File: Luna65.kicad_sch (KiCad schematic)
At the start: 169 parts, among them J1 TYPE-C-31-M12_13, SW0 SW_Push, SW1 Esc, SW10 9, SW11 0, SW12 -, SW13 =, SW14 BSP_200, SW15 Del, SW16 Tab_150, SW17 Q, SW18 W, SW19 E, SW2 1, SW20 R, SW21 T, SW22 Y, SW23 U, SW24 I, SW25 O, SW26 P, SW27 [, SW28 ], SW29 \_150, SW3 2, SW30 Home, SW31 Caps_175, SW32 A, SW33 S, SW34 D, SW35 F, SW36 G, SW37 H, SW38 J, SW39 K, SW4 3, SW40 L, SW41 ;, SW42 ', SW43 Ent_225, SW44 PgUp, SW45 LShft_225, SW46 Z, SW47 X, SW48 C, SW49 V, SW5 4, SW50 B, SW51 N, SW52 M, SW53 ,, SW54 ., SW55 /, SW56 RShft_175, SW57 Up, SW58 End, SW59 LCtrl_125, SW6 5, SW60 Win_125, SW61 LAlt_125, SW62 Space_625, SW63 RAlt, SW64 Fn, SW65 RCtrl, SW66 Left, SW67 Down, SW68 Right, SW7 6, SW8 7, SW9 8, U1 ATmega32U4-AU, U2 USBLC6-2SC6, Y1 16MHz

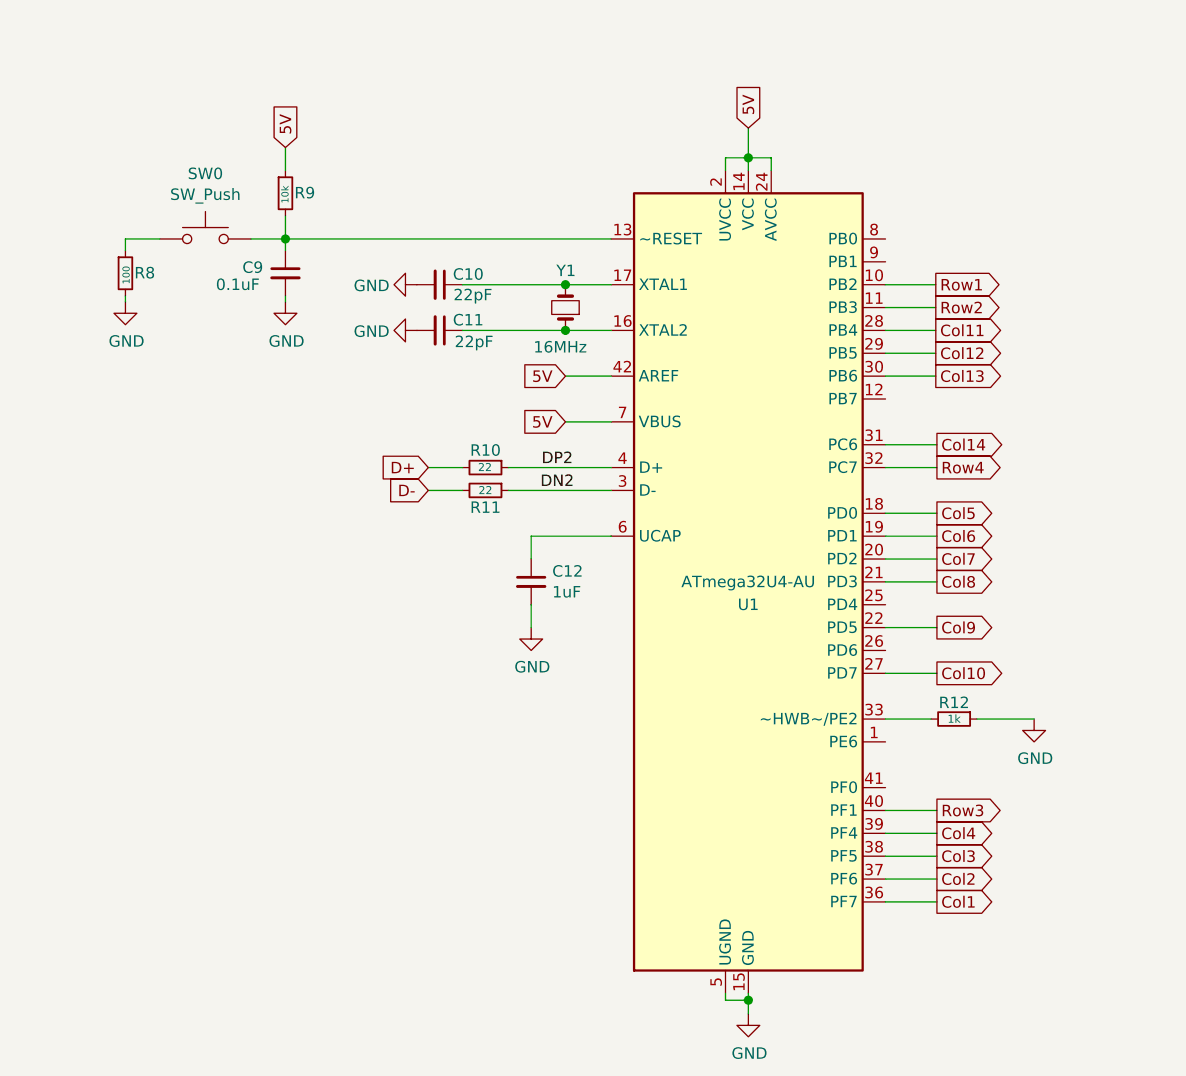
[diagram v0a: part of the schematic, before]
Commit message: Completed routing
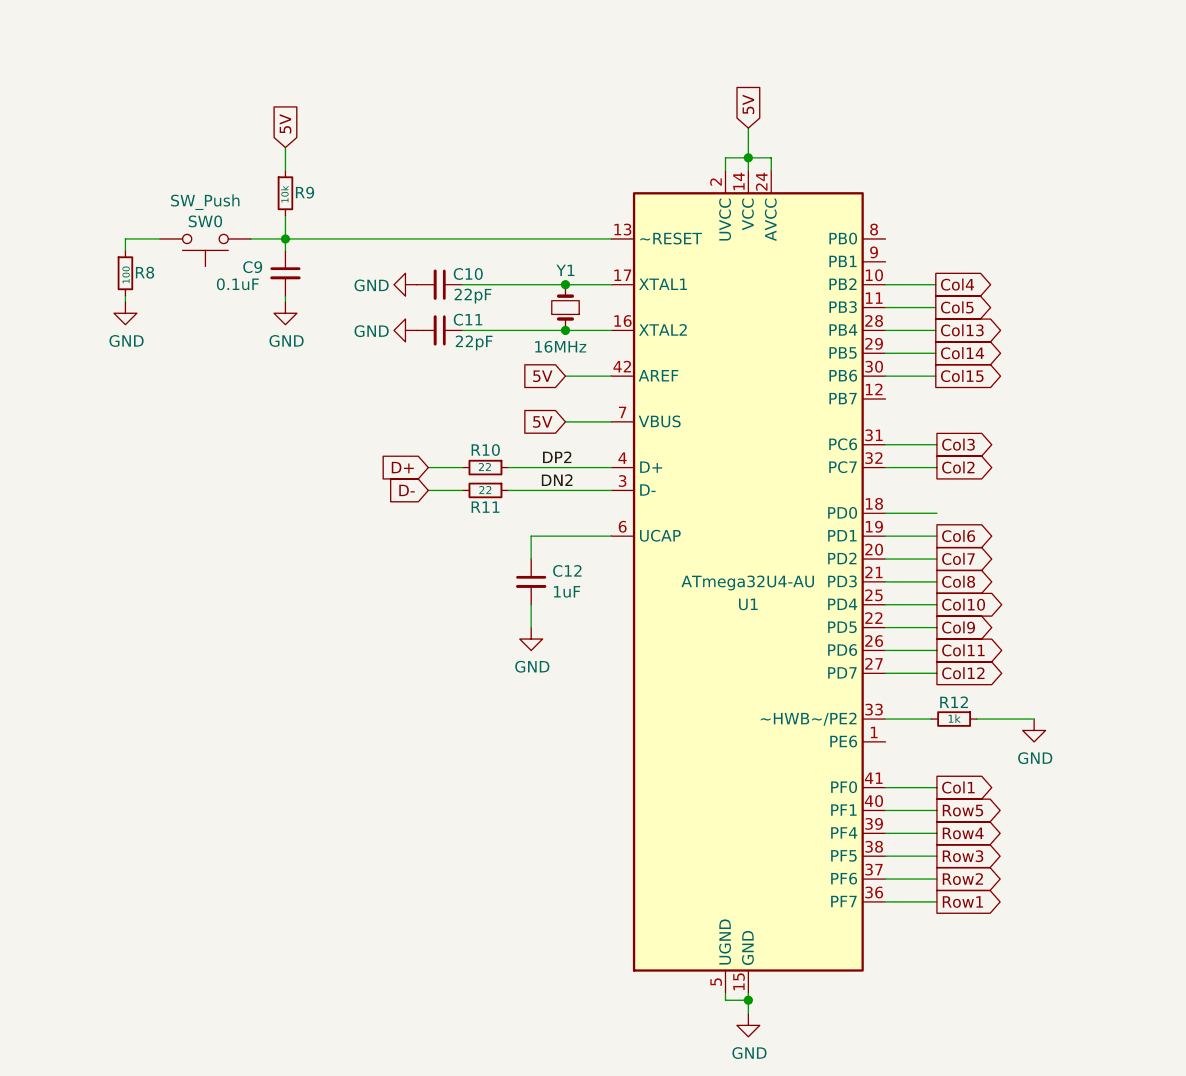
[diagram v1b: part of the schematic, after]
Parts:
- SW0: footprint Button_Switch_SMD:SW_Push_1P1T_NO_CK_KMR2 -> acheron_Hardware:K2-1187SQ-A4SW-06
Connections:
- net Col1: now also U1.41 (PF0); no longer U1.36 (PF7)
- net Col10: now also U1.25 (PD4); no longer U1.27 (PD7)
- net Col11: now also U1.26 (PD6); no longer U1.28 (PB4)
- net Col12: now also U1.27 (PD7); no longer U1.29 (PB5)
- net Col13: now also U1.28 (PB4); no longer U1.30 (PB6)
- net Col14: now also U1.29 (PB5); no longer U1.31 (PC6)
- net Col15: now also U1.30 (PB6)
- net Col2: now also U1.32 (PC7); no longer U1.37 (PF6)
- net Col3: now also U1.31 (PC6); no longer U1.38 (PF5)
- net Col4: now also U1.10 (PB2); no longer U1.39 (PF4)
- net Col5: now also U1.11 (PB3); no longer U1.18 (PD0)
- net Row1: now also U1.36 (PF7); no longer U1.10 (PB2)
- net Row2: now also U1.37 (PF6); no longer U1.11 (PB3)
- net Row3: now also U1.38 (PF5); no longer U1.40 (PF1)
- net Row4: now also U1.39 (PF4); no longer U1.32 (PC7)
- net Row5: now also U1.40 (PF1)
- net at C9.1, R9.2, U1.13 (~RESET): now also SW0.1; no longer SW0.2
- net at R8.1: now also SW0.2; no longer SW0.1
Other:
- moved on the sheet: SW0
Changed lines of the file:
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@@
     (stroke (width 0) (type solid) (color 0 0 0 0))
   )
+  (wire (pts (xy 268.986 223.393) (xy 274.701 223.393))
+    (stroke (width 0) (type solid) (color 0 0 0 0))
+  )
   (wire (pts (xy 268.986 225.933) (xy 274.701 225.933))
     (stroke (width 0) (type solid) (color 0 0 0 0))
   )
+  (wire (pts (xy 268.986 228.473) (xy 274.701 228.473))
+    (stroke (width 0) (type solid) (color 0 0 0 0))
+  )
   (wire (pts (xy 268.986 231.013) (xy 274.701 231.013))
     (stroke (width 0) (type solid) (color 0 0 0 0))
@@
     (stroke (width 0) (type solid) (color 0 0 0 0))
   )
+  (wire (pts (xy 268.986 243.713) (xy 274.701 243.713))
+    (stroke (width 0) (type solid) (color 0 0 0 0))
+  )
   (wire (pts (xy 268.986 246.253) (xy 274.701 246.253))
     (stroke (width 0) (type solid) (color 0 0 0 0))
@@
     )
   )
-  (global_label "Row1" (shape output) (at 274.574 187.833 0) (fields_autoplaced)
+  (global_label "Col4" (shape output) (at 274.574 187.833 0) (fields_autoplaced)
     (effects (font (size 1.27 1.27)) (justify left))
-    (property "Intersheet References" "${INTERSHEET_REFS}" (id 0) (at 281.9461 187.7536 0)
+    (property "Intersheet References" "${INTERSHEET_REFS}" (id 0) (at 281.2809 187.7536 0)
       (effects (font (size 1.27 1.27)) (justify left) hide)
     )
   )
-  (global_label "Row2" (shape output) (at 274.574 190.373 0) (fields_autoplaced)
+  (global_label "Col5" (shape output) (at 274.574 190.373 0) (fields_autoplaced)
     (effects (font (size 1.27 1.27)) (justify left))
-    (property "Intersheet References" "${INTERSHEET_REFS}" (id 0) (at 281.9461 190.2936 0)
+    (property "Intersheet References" "${INTERSHEET_REFS}" (id 0) (at 281.2809 190.2936 0)
       (effects (font (size 1.27 1.27)) (justify left) hide)
     )
   )
-  (global_label "Col11" (shape output) (at 274.574 192.913 0) (fields_autoplaced)
+  (global_label "Col13" (shape output) (at 274.574 192.913 0) (fields_autoplaced)
     (effects (font (size 1.27 1.27)) (justify left))
     (property "Intersheet References" "${INTERSHEET_REFS}" (id 0) (at 282.4904 192.8336 0)
@@
     )
   )
-  (global_label "Col12" (shape output) (at 274.574 195.453 0) (fields_autoplaced)
+  (global_label "Col14" (shape output) (at 274.574 195.453 0) (fields_autoplaced)
     (effects (font (size 1.27 1.27)) (justify left))
     (property "Intersheet References" "${INTERSHEET_REFS}" (id 0) (at 282.4904 195.3736 0)
@@
     )
   )
-  (global_label "Col13" (shape output) (at 274.574 197.993 0) (fields_autoplaced)
+  (global_label "Col15" (shape output) (at 274.574 197.993 0) (fields_autoplaced)
     (effects (font (size 1.27 1.27)) (justify left))
     (property "Intersheet References" "${INTERSHEET_REFS}" (id 0) (at 282.4904 197.9136 0)
@@
     )
   )
-  (global_label "Col14" (shape output) (at 274.701 205.613 0) (fields_autoplaced)
+  (global_label "Col3" (shape output) (at 274.701 205.613 0) (fields_autoplaced)
     (effects (font (size 1.27 1.27)) (justify left))
-    (property "Intersheet References" "${INTERSHEET_REFS}" (id 0) (at 282.6174 205.5336 0)
+    (property "Intersheet References" "${INTERSHEET_REFS}" (id 0) (at 281.4079 205.5336 0)
       (effects (font (size 1.27 1.27)) (justify left) hide)
     )
   )
-  (global_label "Row4" (shape output) (at 274.701 208.153 0) (fields_autoplaced)
+  (global_label "Col2" (shape output) (at 274.701 208.153 0) (fields_autoplaced)
     (effects (font (size 1.27 1.27)) (justify left))
-    (property "Intersheet References" "${INTERSHEET_REFS}" (id 0) (at 282.0731 208.0736 0)
-      (effects (font (size 1.27 1.27)) (justify left) hide)
-    )
-  )
-  (global_label "Col5" (shape output) (at 274.701 213.233 0) (fields_autoplaced)
-    (effects (font (size 1.27 1.27)) (justify left))
-    (property "Intersheet References" "${INTERSHEET_REFS}" (id 0) (at 281.4079 213.1536 0)
+    (property "Intersheet References" "${INTERSHEET_REFS}" (id 0) (at 281.4079 208.0736 0)
       (effects (font (size 1.27 1.27)) (justify left) hide)
     )
@@
     )
   )
+  (global_label "Col10" (shape output) (at 274.701 223.393 0) (fields_autoplaced)
+    (effects (font (size 1.27 1.27)) (justify left))
+    (property "Intersheet References" "${INTERSHEET_REFS}" (id 0) (at 282.6174 223.3136 0)
+      (effects (font (size 1.27 1.27)) (justify left) hide)
+    )
+  )
   (global_label "Col9" (shape output) (at 274.701 225.933 0) (fields_autoplaced)
     (effects (font (size 1.27 1.27)) (justify left))
@@
     )
   )
-  (global_label "Col10" (shape output) (at 274.701 231.013 0) (fields_autoplaced)
+  (global_label "Col11" (shape output) (at 274.701 228.473 0) (fields_autoplaced)
+    (effects (font (size 1.27 1.27)) (justify left))
+    (property "Intersheet References" "${INTERSHEET_REFS}" (id 0) (at 282.6174 228.3936 0)
+      (effects (font (size 1.27 1.27)) (justify left) hide)
+    )
+  )
+  (global_label "Col12" (shape output) (at 274.701 231.013 0) (fields_autoplaced)
     (effects (font (size 1.27 1.27)) (justify left))
     (property "Intersheet References" "${INTERSHEET_REFS}" (id 0) (at 282.6174 230.9336 0)
@@
     )
   )
-  (global_label "Row3" (shape output) (at 274.701 246.253 0) (fields_autoplaced)
+  (global_label "Col1" (shape output) (at 274.701 243.713 0) (fields_autoplaced)
+    (effects (font (size 1.27 1.27)) (justify left))
+    (property "Intersheet References" "${INTERSHEET_REFS}" (id 0) (at 281.4079 243.6336 0)
+      (effects (font (size 1.27 1.27)) (justify left) hide)
+    )
+  )
+  (global_label "Row5" (shape output) (at 274.701 246.253 0) (fields_autoplaced)
     (effects (font (size 1.27 1.27)) (justify left))
     (property "Intersheet References" "${INTERSHEET_REFS}" (id 0) (at 282.0731 246.1736 0)
@@
     )
   )
-  (global_label "Col4" (shape output) (at 274.701 248.793 0) (fields_autoplaced)
+  (global_label "Row4" (shape output) (at 274.701 248.793 0) (fields_autoplaced)
     (effects (font (size 1.27 1.27)) (justify left))
-    (property "Intersheet References" "${INTERSHEET_REFS}" (id 0) (at 281.4079 248.7136 0)
+    (property "Intersheet References" "${INTERSHEET_REFS}" (id 0) (at 282.0731 248.7136 0)
       (effects (font (size 1.27 1.27)) (justify left) hide)
     )
   )
-  (global_label "Col3" (shape output) (at 274.701 251.333 0) (fields_autoplaced)
+  (global_label "Row3" (shape output) (at 274.701 251.333 0) (fields_autoplaced)
     (effects (font (size 1.27 1.27)) (justify left))
-    (property "Intersheet References" "${INTERSHEET_REFS}" (id 0) (at 281.4079 251.2536 0)
+    (property "Intersheet References" "${INTERSHEET_REFS}" (id 0) (at 282.0731 251.2536 0)
       (effects (font (size 1.27 1.27)) (justify left) hide)
     )
   )
-  (global_label "Col2" (shape output) (at 274.701 253.873 0) (fields_autoplaced)
+  (global_label "Row2" (shape output) (at 274.701 253.873 0) (fields_autoplaced)
     (effects (font (size 1.27 1.27)) (justify left))
-    (property "Intersheet References" "${INTERSHEET_REFS}" (id 0) (at 281.4079 253.7936 0)
+    (property "Intersheet References" "${INTERSHEET_REFS}" (id 0) (at 282.0731 253.7936 0)
       (effects (font (size 1.27 1.27)) (justify left) hide)
     )
   )
-  (global_label "Col1" (shape output) (at 274.701 256.413 0) (fields_autoplaced)
+  (global_label "Row1" (shape output) (at 274.701 256.413 0) (fields_autoplaced)
     (effects (font (size 1.27 1.27)) (justify left))
-    (property "Intersheet References" "${INTERSHEET_REFS}" (id 0) (at 281.4079 256.3336 0)
+    (property "Intersheet References" "${INTERSHEET_REFS}" (id 0) (at 282.0731 256.3336 0)
       (effects (font (size 1.27 1.27)) (justify left) hide)
     )
@@
     (pin "2")
   )
-  (symbol (lib_id "Switch:SW_Push") (at 193.421 182.753 0) (unit 1)
+  (symbol (lib_id "Switch:SW_Push") (at 193.421 182.753 180) (unit 1)
     (in_bom yes) (on_board yes)
-    (property "Reference" "SW0" (id 0) (at 193.421 175.514 0))
-    (property "Value" "SW_Push" (id 1) (at 193.421 177.8254 0))
-    (property "Footprint" "Button_Switch_SMD:SW_Push_1P1T_NO_CK_KMR2" (id 2) (at 193.421 177.673 0)
+    (property "Reference" "SW0" (id 0) (at 193.421 180.848 0))
+    (property "Value" "SW_Push" (id 1) (at 193.421 178.5366 0))
+    (property "Footprint" "acheron_Hardware:K2-1187SQ-A4SW-06" (id 2) (at 193.421 187.833 0)
       (effects (font (size 1.27 1.27)) hide)
     )
-    (property "Datasheet" "~" (id 3) (at 193.421 177.673 0)
+    (property "Datasheet" "~" (id 3) (at 193.421 187.833 0)
       (effects (font (size 1.27 1.27)) hide)
     )
@@
     )
     (path "/00000000-0000-0000-0000-000060e6da04"
-      (reference "SW0") (unit 1) (value "SW_Push") (footprint "Button_Switch_SMD:SW_Push_1P1T_NO_CK_KMR2")
+      (reference "SW0") (unit 1) (value "SW_Push") (footprint "acheron_Hardware:K2-1187SQ-A4SW-06")
     )
     (path "/287de41a-5fe1-4585-9030-d67797014729"

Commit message: Schematic fixes. Prep for LEDs
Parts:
- removed R1: 1.5K, acheron_Components:R_SMD_1206, symbol Device:R_Small
- removed R10, R11: 22, acheron_Components:R_SMD_1206, symbol Device:R_Small
- C2: value 100nF -> 0.1uF
- F1: footprint acheron_Components:Fuse_1812_4532 -> Fuse:Fuse_1206_3216Metric_Pad1.42x1.75mm_HandSolder
- U2: footprint acheron_Components:SOT-23-6 -> Package_TO_SOT_SMD:SOT-23-6
- renumbered R12 to R1
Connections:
- net DN2 is gone; now on net D-: U1.3 (D-)
- net DP2 is gone; now on net D+: U1.4 (D+)
- net 5V: now also D70.1 (K); no longer D70.2 (A)
- net GND: now also D70.2 (A); no longer D70.1 (K)
- no-connect marks 2 -> 7
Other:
- moved on the sheet: C1, C10, C11, C12, C13, C2, C3, C4, C5, C6, C7, C8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

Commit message: V3 Changes
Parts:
- added D100, D101, D102, D103, D104, D105, D106, D107, D108, D109, D110, D111, D112, D113, D114, D115, D116, D117, D118, D119, D120, D121, D122, D123, D124, D125, D126, D127, D128, D129, D130, D131, D132, D133, D134, D135, D136, D137, D138, D71, D72, D73, D74, D75, D76, D77, D78, D79, D80, D81, D82, D83, D84, D85, D86, D87, D88, D89, D90, D91, D92, D93, D94, D95, D96, D97, D98, D99: LED_Small, LED_SMD:LED_1206_3216Metric_Pad1.42x1.75mm_HandSolder, symbol Device:LED_Small
- added H1, H10, H11, H12, H2, H3, H4, H5, H6, H7, H8: MountingHole, MountingHole:MountingHole_2.7mm_M2.5_Pad, symbol Mechanical:MountingHole
- added H9: MountingHole_Pad, MountingHole:MountingHole_2.7mm_M2.5_Pad, symbol Mechanical:MountingHole_Pad
- added Q1: DTC123JKAT146, Package_TO_SOT_SMD:SOT-23, symbol acheronSymbols:DTC123J
- added Q2: AO3401A, Package_TO_SOT_SMD:SOT-23, symbol Transistor_FET:AO3401A
- added R10: 1k, acheron_Components:R_SMD_1206, symbol Device:R
- added R11: 100R, acheron_Components:R_SMD_1206, symbol Device:R
- added R12, R13, R14, R15, R16, R17, R18, R19, R20, R21, R22, R23, R24, R25, R26, R27, R28, R29, R30, R31, R32, R33, R34, R35, R36, R37, R38, R39, R40, R41, R42, R43, R44, R45, R46, R47, R48, R49, R50, R51, R52, R53, R54, R55, R56, R57, R58, R59, R60, R61, R62, R63, R64, R65, R66, R67, R68, R69, R70, R71, R72, R73, R74, R75, R76, R77, R78, R79: 420, acheron_Components:R_SMD_1206, symbol Device:R_Small
- D69: value 1N4007 -> 1N4148W
- SW14: footprint acheron_MXH:MX200H -> acheron_MXH:MX200HR
- SW43, SW45: footprint acheron_MXH:MX225H -> acheron_MXH:MX225HR
- SW62: footprint acheron_MXH:MX625H -> acheron_MXH:MX625HR
- Y1: footprint Crystal:Crystal_SMD_5032-2Pin_5.0x3.2mm_HandSoldering -> acheron_Components:Crystal_SMD_5032-2Pin
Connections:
- net 5V: now also Q2.2 (S), R10.2
- net CASE: now also H9.1
- net GND: now also D100.1 (K), D101.1 (K), D102.1 (K), D103.1 (K), D104.1 (K), D105.1 (K), D106.1 (K), D107.1 (K), D108.1 (K), D109.1 (K), D110.1 (K), D111.1 (K), D112.1 (K), D113.1 (K), D114.1 (K), D115.1 (K), D116.1 (K), D117.1 (K), D118.1 (K), D119.1 (K), D120.1 (K), D121.1 (K), D122.1 (K), D123.1 (K), D124.1 (K), D125.1 (K), D126.1 (K), D127.1 (K), D128.1 (K), D129.1 (K), D130.1 (K), D131.1 (K), D132.1 (K), D133.1 (K), D134.1 (K), D135.1 (K), D136.1 (K), D137.1 (K), D138.1 (K), D71.1 (K), D72.1 (K), D73.1 (K), D74.1 (K), D75.1 (K), D76.1 (K), D77.1 (K), D78.1 (K), D79.1 (K), D80.1 (K), D81.1 (K), D82.1 (K), D83.1 (K), D84.1 (K), D85.1 (K), D86.1 (K), D87.1 (K), D88.1 (K), D89.1 (K), D90.1 (K), D91.1 (K), D92.1 (K), D93.1 (K), D94.1 (K), D95.1 (K), D96.1 (K), D97.1 (K), D98.1 (K), D99.1 (K), Q1.2 (E)
- new net: D130.2 (A), R71.2
- new net: D112.2 (A), R53.2
- new net: D71.2 (A), R12.2
- new net: Q2.3 (D), R12.1, R13.1, R14.1, R15.1, R16.1, R17.1, R18.1, R19.1, R20.1, R21.1, R22.1, R23.1, R24.1, R25.1, R26.1, R27.1, R28.1, R29.1, R30.1, R31.1, R32.1, R33.1, R34.1, R35.1, R36.1, R37.1, R38.1, R39.1, R40.1, R41.1, R42.1, R43.1, R44.1, R45.1, R46.1, R47.1, R48.1, R49.1, R50.1, R51.1, R52.1, R53.1, R54.1, R55.1, R56.1, R57.1, R58.1, R59.1, R60.1, R61.1, R62.1, R63.1, R64.1, R65.1, R66.1, R67.1, R68.1, R69.1, R70.1, R71.1, R72.1, R73.1, R74.1, R75.1, R76.1, R77.1, R78.1, R79.1
- new net: D123.2 (A), R64.2
- new net: D118.2 (A), R59.2
- new net: D95.2 (A), R36.2
- new net: D106.2 (A), R47.2
- new net: D135.2 (A), R76.2
- new net: D124.2 (A), R65.2
- new net: D88.2 (A), R29.2
- new net: D92.2 (A), R33.2
- new net: D96.2 (A), R37.2
- new net: D104.2 (A), R45.2
- new net: D127.2 (A), R68.2
- new net: D82.2 (A), R23.2
- new net: D91.2 (A), R32.2
- new net: D119.2 (A), R60.2
- new net: D101.2 (A), R42.2
- new net: D107.2 (A), R48.2
- new net: D116.2 (A), R57.2
- new net: D108.2 (A), R49.2
- new net: D111.2 (A), R52.2
- new net: D87.2 (A), R28.2
- new net: D120.2 (A), R61.2
- new net: D131.2 (A), R72.2
- new net: D136.2 (A), R77.2
- new net: D74.2 (A), R15.2
- new net: D113.2 (A), R54.2
- new net: D79.2 (A), R20.2
- new net: D86.2 (A), R27.2
- new net: D73.2 (A), R14.2
- new net: D133.2 (A), R74.2
- new net: D132.2 (A), R73.2
- new net: D83.2 (A), R24.2
- new net: D114.2 (A), R55.2
- new net: D117.2 (A), R58.2
- new net: D121.2 (A), R62.2
- new net: D89.2 (A), R30.2
- new net: D80.2 (A), R21.2
- new net: D109.2 (A), R50.2
- new net: D134.2 (A), R75.2
- new net: Q1.3 (C), R10.1, R11.2
- new net: D105.2 (A), R46.2
- new net: D103.2 (A), R44.2
- new net: D129.2 (A), R70.2
- new net: D125.2 (A), R66.2
- new net: D85.2 (A), R26.2
- new net: D84.2 (A), R25.2
- new net: D122.2 (A), R63.2
- new net: D126.2 (A), R67.2
- new net: D138.2 (A), R79.2
- new net: D94.2 (A), R35.2
- new net: D115.2 (A), R56.2
- new net: D93.2 (A), R34.2
- new net: D78.2 (A), R19.2
- new net: D72.2 (A), R13.2
- new net: D137.2 (A), R78.2
- new net: D97.2 (A), R38.2
- new net: D81.2 (A), R22.2
- new net: D102.2 (A), R43.2
- new net: D99.2 (A), R40.2
- new net: D100.2 (A), R41.2
- new net: D90.2 (A), R31.2
- new net: Q2.1 (G), R11.1
- new net: D75.2 (A), R16.2
- new net: D77.2 (A), R18.2
- new net: D98.2 (A), R39.2
- new net: D128.2 (A), R69.2
- new net: D76.2 (A), R17.2
- new net: D110.2 (A), R51.2
- new net LED_PWM: Q1.1 (B)
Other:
- moved on the sheet: C1, C10, C11, C12, C13, C2, C3, C4, C5, C6, C7, C8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

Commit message: Done with v3
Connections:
- net Col1: now also U1.36 (PF7); no longer U1.41 (PF0)
- net LED_PWM: now also U1.18 (PD0)
- net Row1: now also U1.37 (PF6); no longer U1.36 (PF7)
- net Row2: now also U1.38 (PF5); no longer U1.37 (PF6)
- net Row3: now also U1.39 (PF4); no longer U1.38 (PF5)
- net Row4: now also U1.40 (PF1); no longer U1.39 (PF4)
- net Row5: now also U1.41 (PF0); no longer U1.40 (PF1)
- no-connect marks 7 -> 6
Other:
- moved on the sheet: H9
